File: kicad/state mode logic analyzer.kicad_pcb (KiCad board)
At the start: 4 copper layers, 64.9 x 64.9 mm, 144 parts, among them J1 USB0, J10 5V USB1, J2 USB1, J3 CLK 0-7, J4 8-15, J5 16-23, J6 24-31, J7 SWD0, J8 SWD1, J9 5V USB0, SW1 Reset 0, SW2 Boot 0, SW3 Reset 1, SW4 Boot 1, U1 RP2040, U2 RP2040, U3 74HC4520D, U4 LTC6994xS6-1, U5 MCP4725, U6 AD5241-1M, U7 IS25LP128F-JBLE, U8 IS25LP128F-JBLE, U9 MCP1826S, Y1 ECS-120-18-33-JEM-TR, Y2 ECS-120-18-33-JEM-TR

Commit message: saving current state to try a different design
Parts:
- moved J6 67.1 mm to (192.5, 124.7)
- moved J3 60.0 mm to (192.5, 42.4)
- moved J5 50.9 mm to (192.5, 97.3)
- moved J4 47.8 mm to (192.5, 69.9)
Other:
- board outline removed
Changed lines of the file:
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@@
   )
   (footprint "Connector_PinHeader_2.54mm:PinHeader_2x10_P2.54mm_Vertical" (layer "F.Cu")
-    (at 152 66.505)
+    (at 192.527 97.287)
     (descr "Through hole straight pin header, 2x10, 2.54mm pitch, double rows")
     (tags "Through hole pin header THT 2x10 2.54mm double row")
@@
   )
   (footprint "Connector_PinHeader_2.54mm:PinHeader_2x10_P2.54mm_Vertical" (layer "F.Cu")
-    (at 144.8 66.505)
+    (at 192.527 69.855)
     (descr "Through hole straight pin header, 2x10, 2.54mm pitch, double rows")
     (tags "Through hole pin header THT 2x10 2.54mm double row")
@@
   )
   (footprint "Connector_PinHeader_2.54mm:PinHeader_2x10_P2.54mm_Vertical" (layer "F.Cu")
-    (at 137.6 66.505)
+    (at 192.527 42.423)
     (descr "Through hole straight pin header, 2x10, 2.54mm pitch, double rows")
     (tags "Through hole pin header THT 2x10 2.54mm double row")
@@
   )
   (footprint "Connector_PinHeader_2.54mm:PinHeader_2x10_P2.54mm_Vertical" (layer "F.Cu")
-    (at 159.2 66.505)
+    (at 192.527 124.719)
     (descr "Through hole straight pin header, 2x10, 2.54mm pitch, double rows")
     (tags "Through hole pin header THT 2x10 2.54mm double row")
@@
     )
   )
-  (gr_rect (start 111.275 61.6) (end 176.225 126.55)
-    (stroke (width 0.1) (type default)) (fill none) (layer "Edge.Cuts"))
 )

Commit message: floor planning ongoing
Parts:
- removed C13, C18: 10u, Capacitor_SMD:C_0805_2012Metric
- removed C14, C15, C16, C17, C26, C27, C28, C29, C30: 1u, Capacitor_SMD:C_0603_1608Metric_Pad1.08x0.95mm_HandSolder
- removed J10: 5V USB1, Connector_PinHeader_2.54mm:PinHeader_1x02_P2.54mm_Vertical
- removed J6: 24-31, Connector_PinHeader_2.54mm:PinHeader_2x10_P2.54mm_Vertical
- removed J8: SWD1, FTSH-105-01-L-DV-K:SAMTEC_FTSH-105-XX-X-DV
- removed SW3: Reset 1, Button_Switch_SMD:SW_SPST_PTS810
- removed SW4: Boot 1, Button_Switch_SMD:SW_SPST_PTS810
- removed TP116, TP117, TP118, TP119, TP120, TP121, TP122, TP123, TP124, TP125, TP126, TP127, TP128, TP129, TP130, TP131, TP132: TestPoint_Harwin, My Libraries:Harwin-S1751-46-Test-Point
- removed Y2: ECS-120-18-33-JEM-TR, Crystal:Crystal_SMD_3225-4Pin_3.2x2.5mm
- added JP6: CLK Bypass, Jumper:SolderJumper-2_P1.3mm_Bridged2Bar_Pad1.0x1.5mm, F.Cu at (162.1, 82.7)
- added R27: 220, Resistor_SMD:R_0603_1608Metric, F.Cu at (187.1, 77.0)
- added R28: 220, Resistor_SMD:R_0603_1608Metric, F.Cu at (187.1, 79.5)
- added R29: 220, Resistor_SMD:R_0603_1608Metric, F.Cu at (187.1, 82.0)
- added R30: 220, Resistor_SMD:R_0603_1608Metric, F.Cu at (187.1, 84.6)
- added R31: 220, Resistor_SMD:R_0603_1608Metric, F.Cu at (187.1, 87.1)
- added R32: 220, Resistor_SMD:R_0603_1608Metric, F.Cu at (187.1, 89.7)
- added R33: 220, Resistor_SMD:R_0603_1608Metric, F.Cu at (187.2, 100.1)
- added R34: 220, Resistor_SMD:R_0603_1608Metric, F.Cu at (187.2, 102.7)
- added R35: 220, Resistor_SMD:R_0603_1608Metric, F.Cu at (187.2, 105.2)
- added R36: 220, Resistor_SMD:R_0603_1608Metric, F.Cu at (187.2, 107.7)
- added R37: 220, Resistor_SMD:R_0603_1608Metric, F.Cu at (187.2, 110.3)
- added R38: 220, Resistor_SMD:R_0603_1608Metric, F.Cu at (187.2, 112.8)
- added R39: 220, Resistor_SMD:R_0603_1608Metric, F.Cu at (187.2, 115.4)
- added R40: 220, Resistor_SMD:R_0603_1608Metric, F.Cu at (187.2, 117.9)
- added TP16: TestPoint_Harwin, My Libraries:Harwin-S1751-46-Test-Point, F.Cu at (137.0, 121.0)
- added TP17: TestPoint_Harwin, My Libraries:Harwin-S1751-46-Test-Point, F.Cu at (180.1, 68.0)
- added TP18: TestPoint_Harwin, My Libraries:Harwin-S1751-46-Test-Point, F.Cu at (180.2, 120.9)
- added TP19: TestPoint_Harwin, My Libraries:Harwin-S1751-46-Test-Point, F.Cu at (123.1, 70.5)
- C10, C11, C12, C8: moved to B.Cu
- C3, C4: value 27p -> 1u; footprint Capacitor_SMD:C_0603_1608Metric -> Capacitor_SMD:C_0603_1608Metric_Pad1.08x0.95mm_HandSolder
- D7: value 2040_L1 -> BZA856AVL; footprint LED_SMD:LED_1206_3216Metric_Pad1.42x1.75mm_HandSolder -> Package_TO_SOT_SMD:SOT-353_SC-70-5
- J2: value USB1 -> Exp Out; footprint Connector_USB:USB_C_Receptacle_GCT_USB4105-xx-A_16P_TopMnt_Horizontal -> Connector_PinHeader_2.54mm:PinHeader_2x10_P2.54mm_Horizontal
- J5: value 16-23 -> Exp In; footprint Connector_PinHeader_2.54mm:PinHeader_2x10_P2.54mm_Vertical -> Connector_PinSocket_2.54mm:PinSocket_2x10_P2.54mm_Horizontal
- R11, R15: value 1k -> 0
- R18, R19: value 27 -> 0
- R25, R26: value 5k1 -> 220; footprint Resistor_SMD:R_0603_1608Metric_Pad0.98x0.95mm_HandSolder -> Resistor_SMD:R_0603_1608Metric
- R9: value 4k7 -> 0
- U2: value RP2040 -> 74LVC244; footprint Package_DFN_QFN:QFN-56-1EP_7x7mm_P0.4mm_EP3.2x3.2mm -> Package_SO:TSSOP-20_4.4x6.5mm_P0.65mm
- U8: value IS25LP128F-JBLE -> 74LVC244; footprint Package_SO:SOIC-8_5.23x5.23mm_P1.27mm -> Package_SO:TSSOP-20_4.4x6.5mm_P0.65mm
- moved U8 74.8 mm to (180.2, 80.7)
- moved TP0 69.6 mm to (166.6, 112.3), turned to -90 degrees
- moved TP114 66.9 mm to (172.6, 115.9)
- moved TP115 66.7 mm to (172.6, 118.5)
- moved TP1 65.5 mm to (163.7, 112.3), turned to -90 degrees
- moved U2 62.9 mm to (180.2, 107.0)
- moved TP2 61.5 mm to (160.8, 112.3), turned to -90 degrees
- moved SW2 59.3 mm to (121.8, 109.2), turned to -90 degrees
- moved SW1 59.3 mm to (126.2, 109.2), turned to -90 degrees
- moved TP3 57.4 mm to (158.0, 112.3), turned to -90 degrees
- moved TP103 54.4 mm to (172.6, 80.5)
- moved TP102 54.3 mm to (172.6, 77.8)
- moved TP101 54.3 mm to (172.6, 75.2)
- moved TP100 54.2 mm to (172.6, 72.5)
- moved TP11 53.8 mm to (160.7, 103.1)
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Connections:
- C3 pad 1: /XIN0 -> +3V3
- C3 pad 2: Net-(C3-Pad2) -> GND
- C4 pad 1: Net-(C4-Pad1) -> +3V3
- C4 pad 2: Net-(C3-Pad2) -> GND
- D7 pad 1: GND -> unconnected-(D7-K-Pad1)
- D7 pad 2: Net-(D7-A) -> GND
- J1 pad A4: Net-(J9-Pin_2) -> /VBUS
- J1 pad A9: Net-(J9-Pin_2) -> /VBUS
- J1 pad B4: Net-(J9-Pin_2) -> /VBUS
- J1 pad B9: Net-(J9-Pin_2) -> /VBUS
- J5 pad 1: +5V -> /TS0
- J5 pad 10: GND -> unconnected-(J5-Pin_10-Pad10)
- J5 pad 11: /IN20 -> /TS5
- J5 pad 12: GND -> unconnected-(J5-Pin_12-Pad12)
- J5 pad 13: /IN21 -> /TS6
- J5 pad 14: GND -> unconnected-(J5-Pin_14-Pad14)
- J5 pad 15: /IN22 -> /TS7
- J5 pad 16: GND -> unconnected-(J5-Pin_16-Pad16)
- J5 pad 17: /IN23 -> /SDA
- J5 pad 18: GND -> unconnected-(J5-Pin_18-Pad18)
- J5 pad 19: +3V3 -> /SCL
- J5 pad 2: GND -> /CLK
- J5 pad 20: GND -> unconnected-(J5-Pin_20-Pad20)
- J5 pad 3: /IN16 -> /TS1
- J5 pad 4: GND -> /LA_Enable
- J5 pad 5: /IN17 -> /TS2
- J5 pad 6: GND -> unconnected-(J5-Pin_6-Pad6)
- J5 pad 7: /IN18 -> /TS3
- J5 pad 8: GND -> unconnected-(J5-Pin_8-Pad8)
- J5 pad 9: /IN19 -> /TS4
- J9 pad 2: Net-(J9-Pin_2) -> /VBUS
- R11 pad 1: /SS1 -> Net-(U3A-Reset)
- R11 pad 2: Net-(R11-Pad2) -> /CNT_RESET
- R13 pad 1: /XOUT0 -> Net-(U6-SCL)
- R13 pad 2: Net-(C4-Pad1) -> /SCL
- R14 pad 1: Net-(U1-GPIO28_ADC2) -> /CNT_RESET
- R15 pad 1: /CNT_RESET -> Net-(U6-SDA)
- R15 pad 2: Net-(D7-A) -> /SDA
- R18 pad 1: /D1M -> Net-(U5-SCL)
- R18 pad 2: /USB1_DM -> /SCL
- R19 pad 1: /D1P -> Net-(U5-SDA)
- R19 pad 2: /USB1_DP -> /SDA
- R25 pad 1: Net-(J2-CC1) -> /IN00
- R25 pad 2: GND -> Net-(U8-1A0)
- R26 pad 1: Net-(J2-CC2) -> /IN01
- R26 pad 2: GND -> Net-(U8-1A1)
- R9 pad 1: +3V3 -> Net-(U3A-CK)
- R9 pad 2: /Run1 -> /CNT_CLK
- TP10 pad 1: /CNT_CLK -> Net-(U3A-CK)
- TP100 pad 1: /IN00 -> /BUF00
- TP101 pad 1: /IN01 -> /BUF01
- TP102 pad 1: /IN02 -> /BUF02
- TP103 pad 1: /IN03 -> /BUF03
- TP104 pad 1: /IN04 -> /BUF04
- TP105 pad 1: /IN05 -> /BUF05
- TP106 pad 1: /IN06 -> /BUF06
- TP107 pad 1: /IN07 -> /BUF07
- TP108 pad 1: /IN08 -> /BUF08
- TP109 pad 1: /IN09 -> /BUF09
- TP11 pad 1: /CNT_RESET -> Net-(U3A-Reset)
- TP110 pad 1: /IN10 -> /BUF10
- TP111 pad 1: /IN11 -> /BUF11
- TP112 pad 1: /IN12 -> /BUF12
- TP113 pad 1: /IN13 -> /BUF13
- TP114 pad 1: /IN14 -> /BUF14
- TP115 pad 1: /IN15 -> /BUF15
- TP15 pad 1: Net-(U1-GPIO27_ADC1) -> /CNT_CLK
- U1 pad 11: /IN05 -> /BUF05
- U1 pad 12: /IN06 -> /BUF06
- U1 pad 13: /IN07 -> /BUF07
- U1 pad 14: /IN08 -> /BUF08
- U1 pad 15: /IN09 -> /BUF09
- U1 pad 16: /IN10 -> /BUF10
- U1 pad 17: /IN11 -> /BUF11
- U1 pad 18: /IN12 -> /BUF12
- U1 pad 27: /IN13 -> /BUF13
- U1 pad 28: /IN14 -> /BUF14
- U1 pad 29: /IN15 -> /BUF15
- U1 pad 39: Net-(U1-GPIO27_ADC1) -> /CNT_CLK
- U1 pad 40: Net-(U1-GPIO28_ADC2) -> /CNT_RESET
- U1 pad 5: /IN00 -> /BUF00
- U1 pad 6: /IN01 -> /BUF01
- U1 pad 7: /IN02 -> /BUF02
- U1 pad 8: /IN03 -> /BUF03
- U1 pad 9: /IN04 -> /BUF04
- U2 pad 1: +3V3 -> GND
- U2 pad 10: +3V3 -> GND
- U2 pad 11: /IN21 -> Net-(U2-2A3)
- U2 pad 12: /IN22 -> /BUF11
- U2 pad 13: /IN23 -> Net-(U2-2A2)
- U2 pad 14: /IN24 -> /BUF10
- U2 pad 15: /IN25 -> Net-(U2-2A1)
- U2 pad 16: /IN26 -> /BUF09
- U2 pad 17: /IN27 -> Net-(U2-2A0)
- U2 pad 18: /IN28 -> /BUF08
- U2 pad 2: /SDA -> Net-(U2-1A0)
- U2 pad 20: /XIN0 -> +3V3
- U2 pad 3: /SCL -> /BUF12
- U2 pad 4: /CLK -> Net-(U2-1A1)
- U2 pad 5: /IN16 -> /BUF13
- U2 pad 6: /IN17 -> Net-(U2-1A2)
- U2 pad 7: /IN18 -> /BUF14
- U2 pad 8: /IN19 -> Net-(U2-1A3)
- U2 pad 9: /IN20 -> /BUF15
- U3 pad 1: /CNT_CLK -> Net-(U3A-CK)
- U3 pad 15: /CNT_RESET -> Net-(U3A-Reset)
- U3 pad 7: /CNT_RESET -> Net-(U3A-Reset)
- U5 pad 4: /SDA -> Net-(U5-SDA)
- U5 pad 5: /SCL -> Net-(U5-SCL)
- U6 pad 6: /SCL -> Net-(U6-SCL)
- U6 pad 7: /SDA -> Net-(U6-SDA)
- U8 pad 1: /SS1 -> GND
- U8 pad 2: Net-(U2-QSPI_SD1) -> Net-(U8-1A0)
- U8 pad 3: Net-(U2-QSPI_SD2) -> /BUF04
- U8 pad 4: GND -> Net-(U8-1A1)
- U8 pad 5: Net-(U2-QSPI_SD0) -> /BUF05
- U8 pad 6: Net-(U2-QSPI_SCLK) -> Net-(U8-1A2)
- U8 pad 7: Net-(U2-QSPI_SD3) -> /BUF06
- U8 pad 8: +3V3 -> Net-(U8-1A3)
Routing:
- net /IN00: track 0.00 -> 5.04 mm
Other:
- board outline added: 80.7 x 56.7 mm

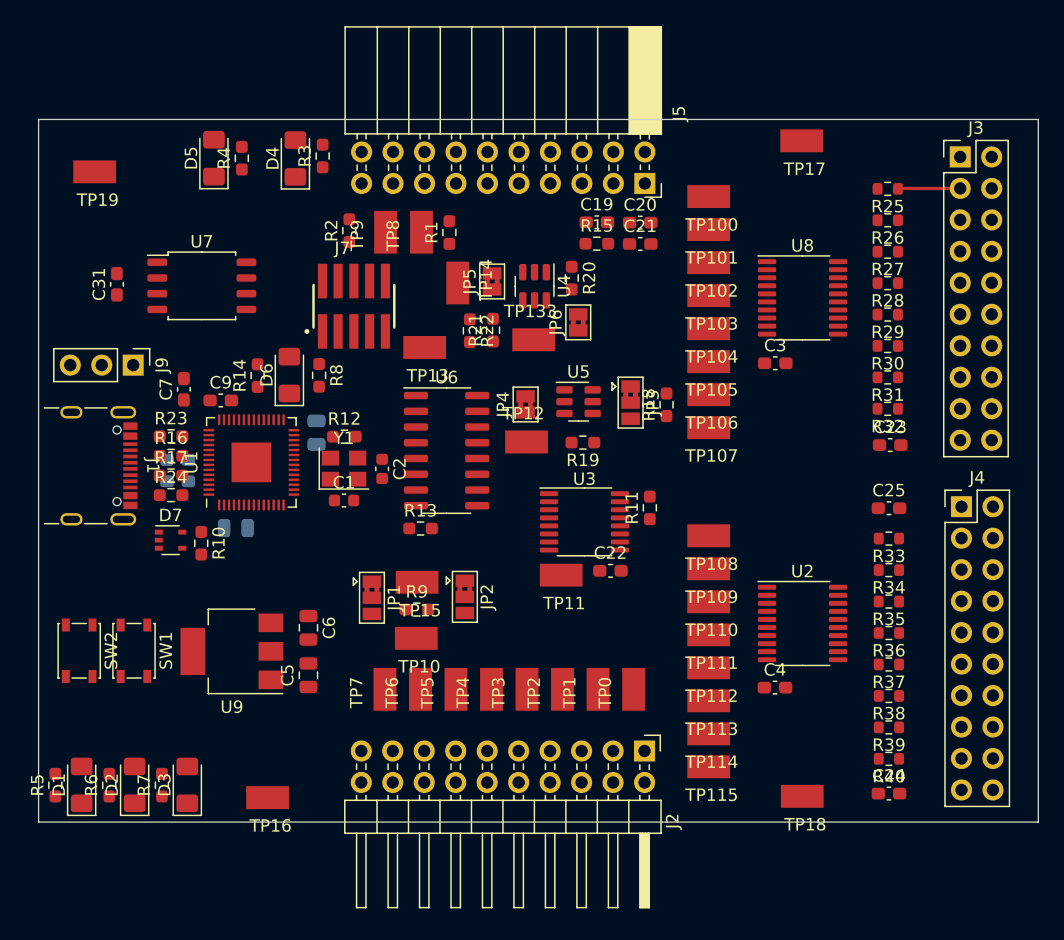
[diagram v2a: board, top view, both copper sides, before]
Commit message: going to re-order all the IOs
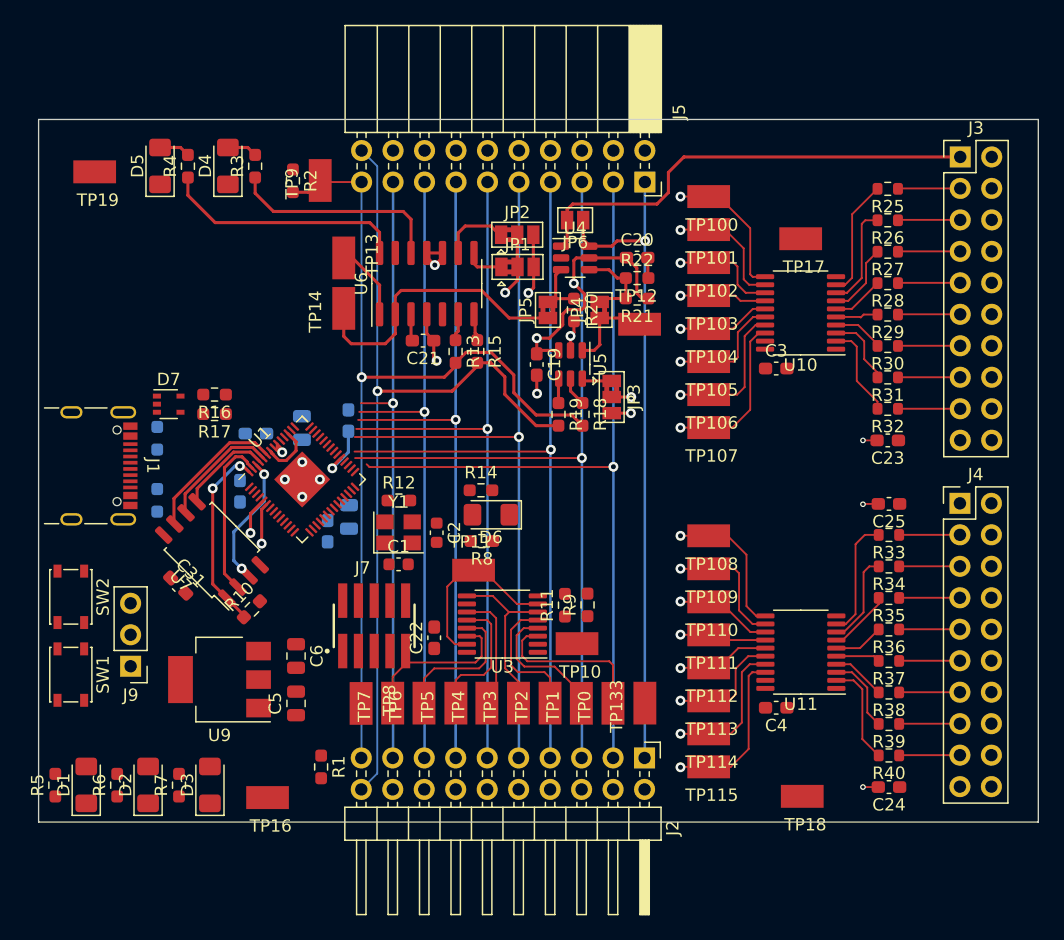
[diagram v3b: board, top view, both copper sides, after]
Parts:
- removed TP15: TestPoint_Harwin, My Libraries:Harwin-S1751-46-Test-Point
- removed U2, U8: 74LVC244, Package_SO:TSSOP-20_4.4x6.5mm_P0.65mm
- added U10: 74LVC245APW, Package_SO:TSSOP-20_4.4x6.5mm_P0.65mm, F.Cu at (180.0, 81.9)
- added U11: 74LVC245APW, Package_SO:TSSOP-20_4.4x6.5mm_P0.65mm, F.Cu at (180.1, 109.3)
- C7, C9, R23, R24: moved to B.Cu
- JP6: footprint Jumper:SolderJumper-2_P1.3mm_Bridged2Bar_Pad1.0x1.5mm -> Jumper:SolderJumper-2_P1.3mm_Open_Pad1.0x1.5mm
- U6: value AD5241-1M -> AD5241BRZ1M; footprint Package_SO:SOIC-16_3.9x9.9mm_P1.27mm -> Package_SO:SOIC-14_3.9x8.7mm_P1.27mm
- moved R1 44.3 mm to (141.3, 118.5), turned to -90 degrees
- moved TP8 38.3 mm to (144.6, 113.4), turned to 90 degrees
- moved TP133 30.7 mm to (167.5, 113.4), turned to -90 degrees
- moved JP2 29.5 mm to (157.2, 75.6), turned to 0 degrees
- moved JP1 29.2 mm to (157.2, 78.2), turned to 0 degrees
- moved J7 25.8 mm to (145.6, 107.2)
- moved C31 24.8 mm to (129.8, 103.9), turned to -45 degrees
- moved J9 24.3 mm to (126.0, 110.4), turned to 180 degrees
- moved U7 21.3 mm to (132.5, 101.0), turned to 135 degrees
- moved R14 20.3 mm to (154.2, 96.2), turned to 0 degrees
- moved D6 19.8 mm to (155.1, 98.2), turned to 180 degrees
- moved C21 19.2 mm to (149.6, 84.2), turned to 180 degrees
- moved R8 18.7 mm to (154.3, 100.3), turned to 180 degrees
- moved C22 15.2 mm to (150.5, 108.1), turned to 90 degrees
- moved R13 14.6 mm to (152.2, 85.0), turned to -90 degrees
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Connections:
- net /D0M renamed /DN
- net /D0P renamed /DP
- net /Run0 renamed /Run
- net /SS0 renamed /~{CS}
- net /SWCLK0 renamed /SWCLK
- net /SWD0 renamed /SWD
- net /USB0_DM renamed /USB_DN
- net /USB0_DP renamed /USB_DP
- net /XIN0 renamed /XIN
- net /XOUT0 renamed /XOUT
- net Net-(JP5-A) renamed /W
- J2 pad 1: /TS0 -> /CLK
- J2 pad 10: unconnected-(J2-Pin_10-Pad10) -> GND
- J2 pad 11: /TS5 -> /TS4
- J2 pad 12: unconnected-(J2-Pin_12-Pad12) -> GND
- J2 pad 13: /TS6 -> /TS5
- J2 pad 14: unconnected-(J2-Pin_14-Pad14) -> GND
- J2 pad 15: /TS7 -> /TS6
- J2 pad 16: unconnected-(J2-Pin_16-Pad16) -> GND
- J2 pad 17: /SDA -> /TS7
- J2 pad 18: unconnected-(J2-Pin_18-Pad18) -> GND
- J2 pad 2: /CLK -> GND
- J2 pad 20: unconnected-(J2-Pin_20-Pad20) -> /SDA
- J2 pad 3: /TS1 -> /TS0
- J2 pad 5: /TS2 -> /TS1
- J2 pad 6: unconnected-(J2-Pin_6-Pad6) -> GND
- J2 pad 7: /TS3 -> /TS2
- J2 pad 8: unconnected-(J2-Pin_8-Pad8) -> GND
- J2 pad 9: /TS4 -> /TS3
- J5 pad 1: /TS0 -> /CLK
- J5 pad 10: unconnected-(J5-Pin_10-Pad10) -> GND
- J5 pad 11: /TS5 -> /TS4
- J5 pad 12: unconnected-(J5-Pin_12-Pad12) -> GND
- J5 pad 13: /TS6 -> /TS5
- J5 pad 14: unconnected-(J5-Pin_14-Pad14) -> GND
- J5 pad 15: /TS7 -> /TS6
- J5 pad 16: unconnected-(J5-Pin_16-Pad16) -> GND
- J5 pad 17: /SDA -> /TS7
- J5 pad 18: unconnected-(J5-Pin_18-Pad18) -> GND
- J5 pad 2: /CLK -> GND
- J5 pad 20: unconnected-(J5-Pin_20-Pad20) -> /SDA
- J5 pad 3: /TS1 -> /TS0
- J5 pad 5: /TS2 -> /TS1
- J5 pad 6: unconnected-(J5-Pin_6-Pad6) -> GND
- J5 pad 7: /TS3 -> /TS2
- J5 pad 8: unconnected-(J5-Pin_8-Pad8) -> GND
- J5 pad 9: /TS4 -> /TS3
- R25 pad 2: Net-(U8-1A0) -> /A0
- R26 pad 2: Net-(U8-1A1) -> /A1
- R27 pad 2: Net-(U8-1A2) -> /A2
- R28 pad 2: Net-(U8-1A3) -> /A3
- R29 pad 2: Net-(U8-2A0) -> /A4
- R30 pad 2: Net-(U8-2A1) -> /A5
- R31 pad 2: Net-(U8-2A2) -> /A6
- R32 pad 2: Net-(U8-2A3) -> /A7
- R33 pad 2: Net-(U2-1A0) -> /A8
- R34 pad 2: Net-(U2-1A1) -> /A9
- R35 pad 2: Net-(U2-1A2) -> /A10
- R36 pad 2: Net-(U2-1A3) -> /A11
- R37 pad 2: Net-(U2-2A0) -> /A12
- R38 pad 2: Net-(U2-2A1) -> /A13
- R39 pad 2: Net-(U2-2A2) -> /A14
- R40 pad 2: Net-(U2-2A3) -> /A15
- U1 pad 11: /BUF05 -> /BUF10
- U1 pad 12: /BUF06 -> /BUF09
- U1 pad 13: /BUF07 -> /BUF08
- U1 pad 14: /BUF08 -> /BUF07
- U1 pad 15: /BUF09 -> /BUF06
- U1 pad 16: /BUF10 -> /BUF05
- U1 pad 17: /BUF11 -> /BUF04
- U1 pad 18: /BUF12 -> /BUF03
- U1 pad 27: /BUF13 -> /BUF02
- U1 pad 28: /BUF14 -> /BUF01
- U1 pad 29: /BUF15 -> /BUF00
- U1 pad 5: /BUF00 -> /BUF15
- U1 pad 6: /BUF01 -> /BUF14
- U1 pad 7: /BUF02 -> /BUF13
- U1 pad 8: /BUF03 -> /BUF12
- U1 pad 9: /BUF04 -> /BUF11
- U9 pad 4: (no net) -> GND
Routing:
- net /TS0: track 0.00 -> 79.9 mm, vias 0 -> 1
- net /TS1: track 0.00 -> 75.8 mm, vias 0 -> 1
- net /TS3: track 0.00 -> 74.7 mm, vias 0 -> 1
- net /SCL: track 0.00 -> 74.6 mm, vias 0 -> 1
- net /TS2: track 0.00 -> 73.4 mm, vias 0 -> 1
- net /SDA: track 0.00 -> 71.2 mm, vias 0 -> 1
- net /BUF07: track 0.00 -> 69.6 mm, vias 0 -> 1
- net /TS4: track 0.00 -> 66.8 mm, vias 0 -> 1
- net /TS5: track 0.00 -> 65.1 mm, vias 0 -> 1
- net /TS6: track 0.00 -> 63.3 mm, vias 0 -> 1
- net /TS7: track 0.00 -> 61.8 mm, vias 0 -> 1
- net /BUF00: track 0.00 -> 59.9 mm, vias 0 -> 1
- net /BUF06: track 0.00 -> 54.7 mm, vias 0 -> 1
- net /CLK: track 0.00 -> 53.5 mm, vias 0 -> 1
- net /BUF05: track 0.00 -> 51.5 mm, vias 0 -> 1
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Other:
- board text added: "need to setup Z for diff pair"
